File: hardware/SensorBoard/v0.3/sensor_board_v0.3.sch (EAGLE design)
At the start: 58 parts, among them IC1 MCP1703CB, IC2 MCP1703CB, J3 USB-MICROB, Q1 MMBT5088-NPN, U1 ATMEGA328P, U2 TSL2561FN, U4 MPL115A, U5 FT231XS, Y1 16MHZ

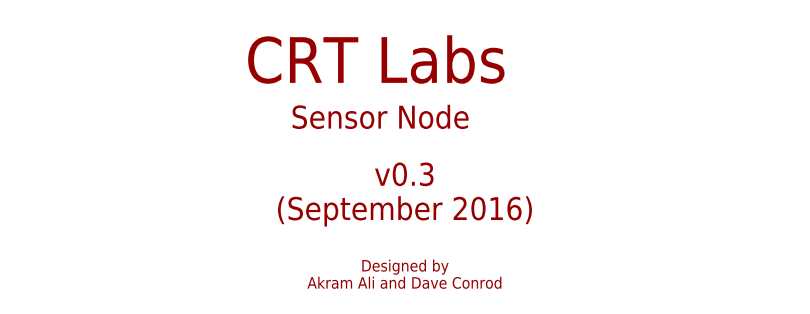
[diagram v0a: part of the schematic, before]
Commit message: modifying v3 enclosure and fixing typo on sensor board v3 schematic
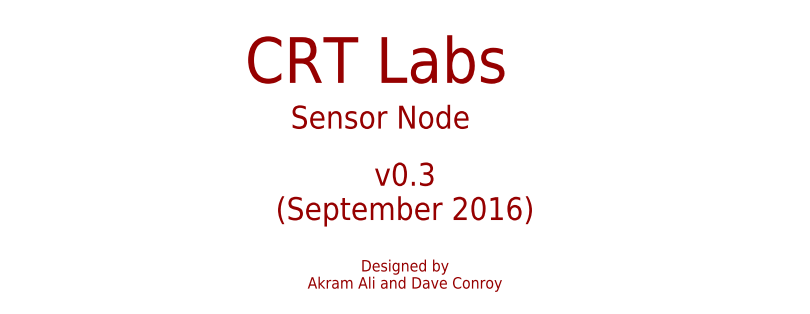
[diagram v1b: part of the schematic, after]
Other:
- note added: "Designed by Akram Ali and Dave Conroy"
- note removed: "Designed by Akram Ali and Dave Conrod"
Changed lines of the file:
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@@
 <?xml version="1.0" encoding="utf-8"?>
 <!DOCTYPE eagle SYSTEM "eagle.dtd">
-<eagle version="7.6.0">
+<eagle version="7.5.0">
 <drawing>
 <settings>
@@
 (September 2016)</text>
 <text x="160.02" y="-175.26" size="1.27" layer="94" font="vector" ratio="10" align="bottom-center">Designed by
-Akram Ali and Dave Conrod</text>
+Akram Ali and Dave Conroy</text>
 <text x="162.56" y="-83.82" size="3.81" layer="94">5V voltage regulator</text>
 <text x="68.58" y="58.42" size="3.81" layer="94">RFM69HW</text>

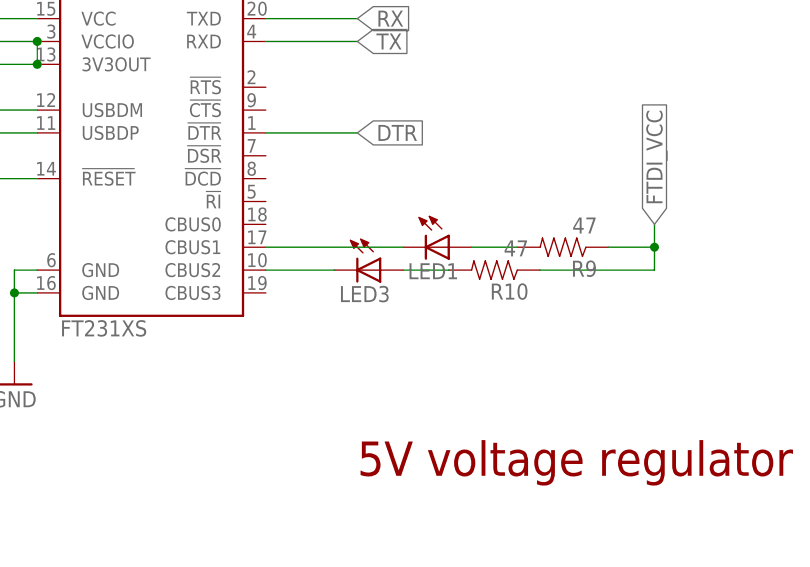
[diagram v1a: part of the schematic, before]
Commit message: Moved labels to _tsilk layer (121)
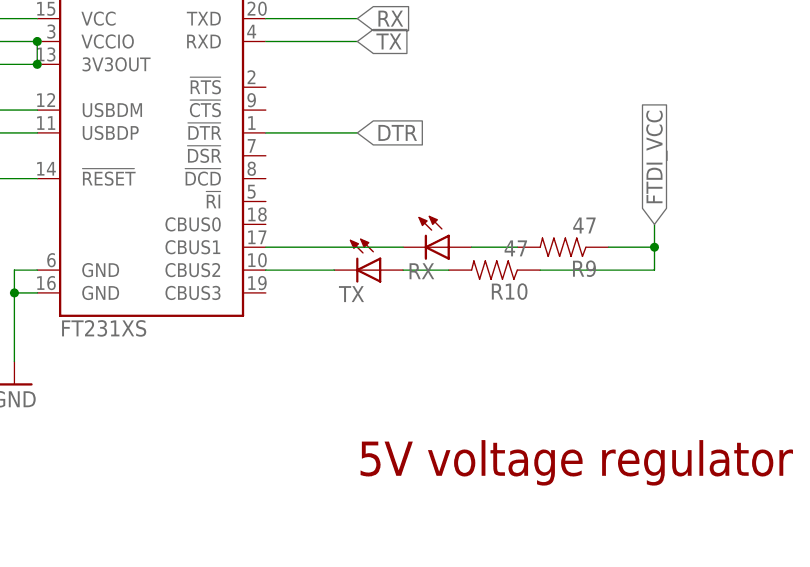
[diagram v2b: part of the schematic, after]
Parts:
- renumbered LED1 to RX, LED3 to TX
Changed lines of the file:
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@@
 <?xml version="1.0" encoding="utf-8"?>
 <!DOCTYPE eagle SYSTEM "eagle.dtd">
-<eagle version="7.5.0">
+<eagle version="7.6.0">
 <drawing>
 <settings>
@@
 <part name="J3" library="SparkFun-Connectors" deviceset="USB" device="-MICROB"/>
 <part name="U5" library="SparkFun-DigitalIC" deviceset="FT231X" device="S" value="FT231XS"/>
-<part name="LED1" library="adafruit" deviceset="LED" device="CHIPLED_0805">
-<attribute name="MF" value=""/>
-<attribute name="MPN" value=""/>
-<attribute name="OC_NEWARK" value="unknown"/>
-</part>
-<part name="LED3" library="adafruit" deviceset="LED" device="CHIPLED_0805">
+<part name="RX" library="adafruit" deviceset="LED" device="CHIPLED_0805">
+<attribute name="MF" value=""/>
+<attribute name="MPN" value=""/>
+<attribute name="OC_NEWARK" value="unknown"/>
+</part>
+<part name="TX" library="adafruit" deviceset="LED" device="CHIPLED_0805">
 <attribute name="MF" value=""/>
 <attribute name="MPN" value=""/>
@@
 <instance part="J3" gate="G$1" x="78.74" y="-30.48" rot="R180"/>
 <instance part="U5" gate="U$1" x="139.7" y="-48.26"/>
-<instance part="LED1" gate="G$1" x="172.72" y="-58.42" rot="R270">
+<instance part="RX" gate="G$1" x="172.72" y="-58.42" rot="R270">
 <attribute name="OC_NEWARK" x="172.72" y="-58.42" size="1.778" layer="96" rot="R90" display="off"/>
 <attribute name="MF" x="172.72" y="-58.42" size="1.778" layer="96" rot="R90" display="off"/>
 <attribute name="MPN" x="172.72" y="-58.42" size="1.778" layer="96" rot="R90" display="off"/>
 </instance>
-<instance part="LED3" gate="G$1" x="165.1" y="-60.96" rot="R270">
+<instance part="TX" gate="G$1" x="165.1" y="-60.96" rot="R270">
 <attribute name="OC_NEWARK" x="165.1" y="-60.96" size="1.778" layer="96" rot="R90" display="off"/>
 <attribute name="MF" x="165.1" y="-60.96" size="1.778" layer="96" rot="R90" display="off"/>
@@
 <segment>
 <pinref part="U5" gate="U$1" pin="CBUS1"/>
-<pinref part="LED1" gate="G$1" pin="C"/>
+<pinref part="RX" gate="G$1" pin="C"/>
 <wire x1="152.4" y1="-58.42" x2="167.64" y2="-58.42" width="0.1524" layer="91"/>
 </segment>
@@
 <segment>
 <pinref part="U5" gate="U$1" pin="CBUS2"/>
-<pinref part="LED3" gate="G$1" pin="C"/>
+<pinref part="TX" gate="G$1" pin="C"/>
 <wire x1="152.4" y1="-60.96" x2="160.02" y2="-60.96" width="0.1524" layer="91"/>
 </segment>
@@
 <net name="N$27" class="0">
 <segment>
-<pinref part="LED1" gate="G$1" pin="A"/>
+<pinref part="RX" gate="G$1" pin="A"/>
 <pinref part="R9" gate="G$1" pin="2"/>
 <wire x1="175.26" y1="-58.42" x2="180.34" y2="-58.42" width="0.1524" layer="91"/>
@@
 <net name="N$29" class="0">
 <segment>
-<pinref part="LED3" gate="G$1" pin="A"/>
+<pinref part="TX" gate="G$1" pin="A"/>
 <pinref part="R10" gate="G$1" pin="2"/>
 <wire x1="167.64" y1="-60.96" x2="172.72" y2="-60.96" width="0.1524" layer="91"/>

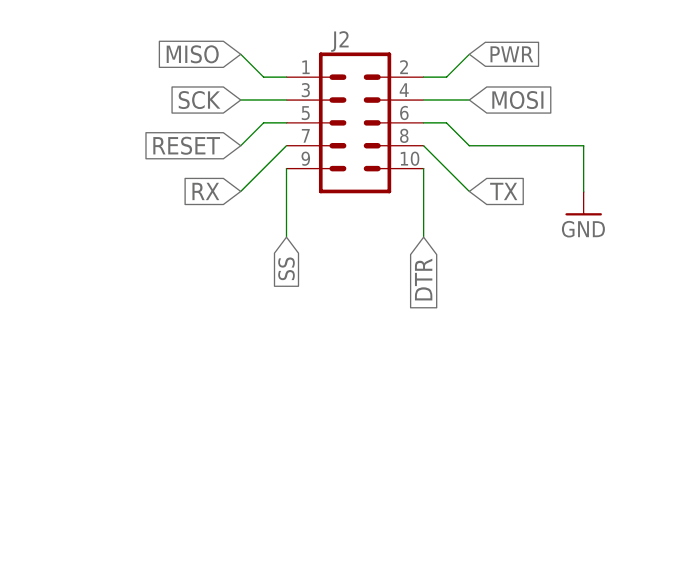
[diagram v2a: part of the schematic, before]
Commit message: Adjusted some traces
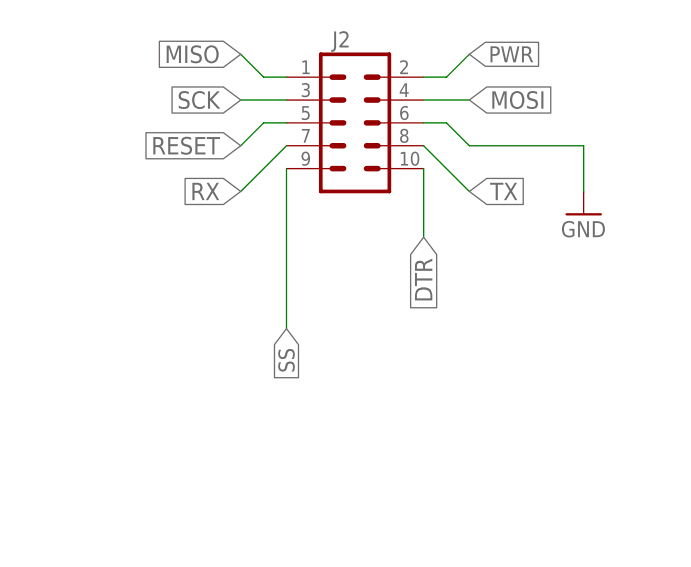
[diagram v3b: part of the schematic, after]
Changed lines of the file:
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@@
 <segment>
 <pinref part="J2" gate="G$1" pin="9"/>
-<wire x1="-40.64" y1="106.68" x2="-40.64" y2="99.06" width="0.1524" layer="91"/>
-<label x="-40.64" y="99.06" size="1.778" layer="95" rot="R270" xref="yes"/>
+<wire x1="-40.64" y1="106.68" x2="-40.64" y2="88.9" width="0.1524" layer="91"/>
+<label x="-40.64" y="88.9" size="1.778" layer="95" rot="R270" xref="yes"/>
 </segment>
 <segment>
